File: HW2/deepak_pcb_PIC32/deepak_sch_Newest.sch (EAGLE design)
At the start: 23 parts, among them J1 USB-MB-H

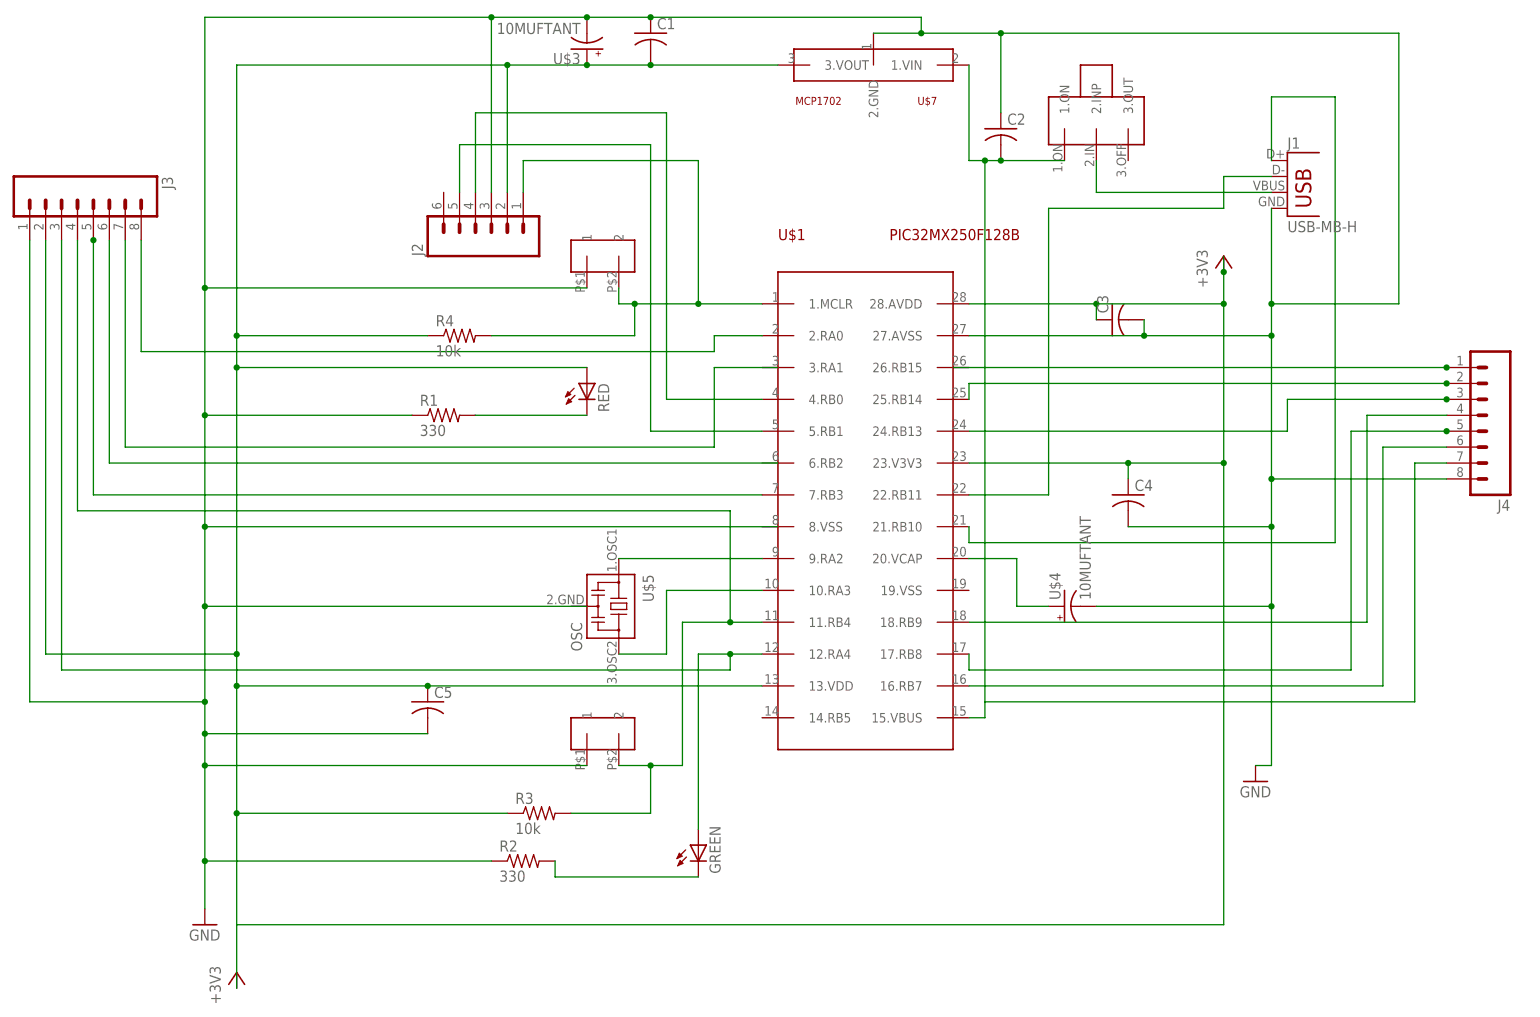
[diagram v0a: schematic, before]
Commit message: Final Schematic. No long connections
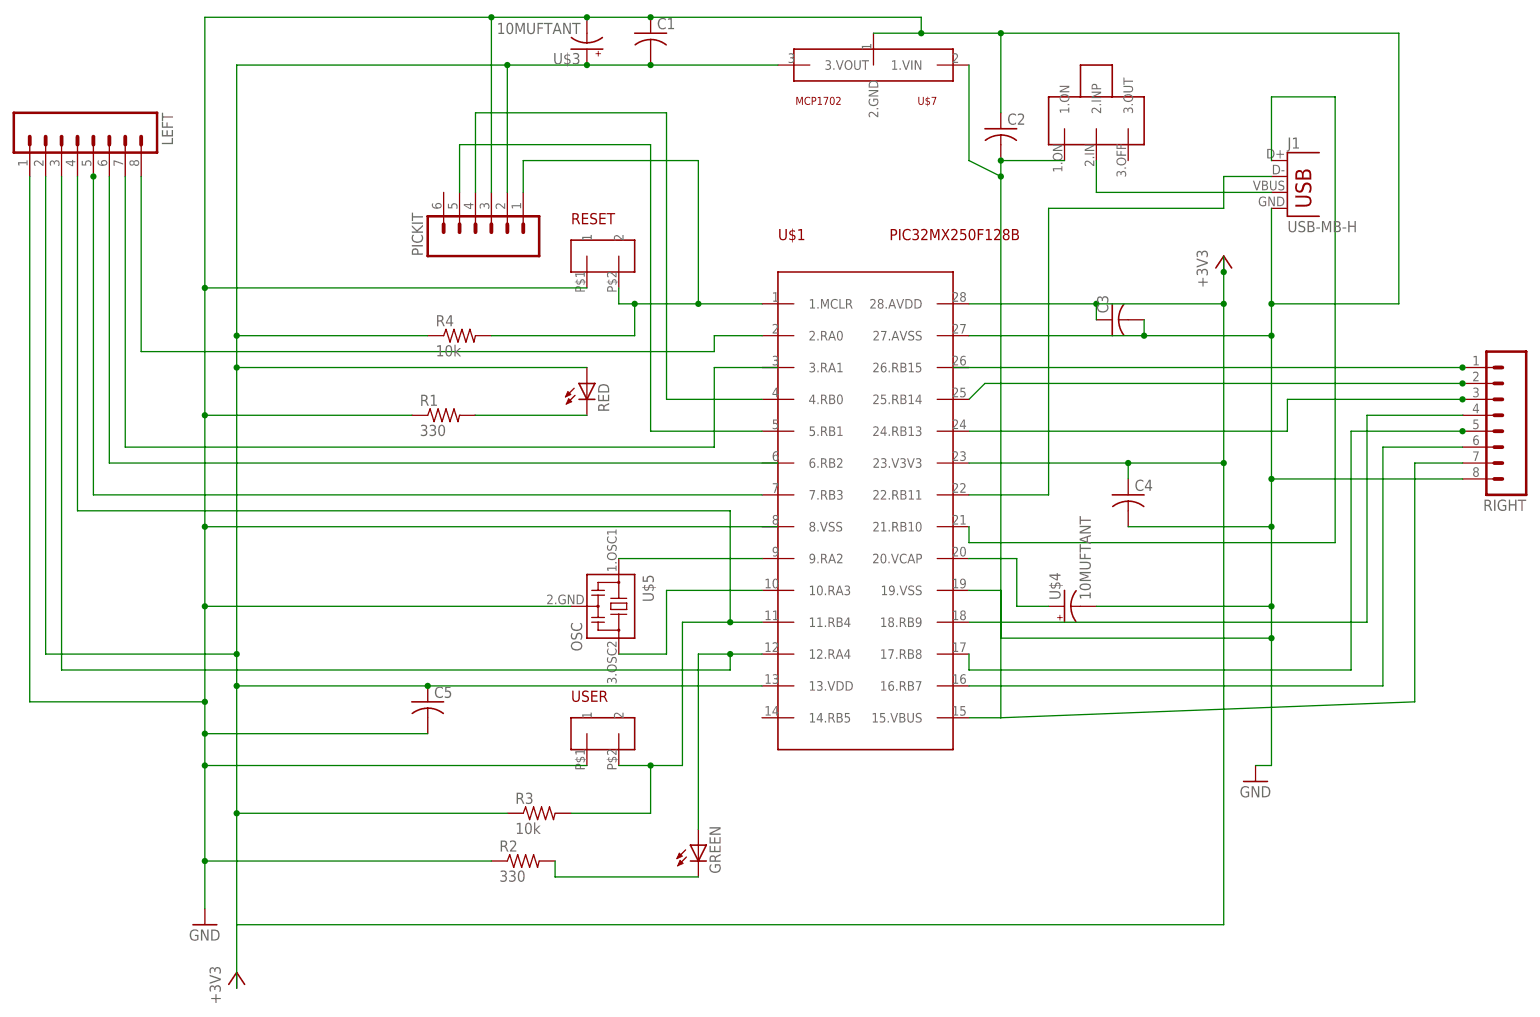
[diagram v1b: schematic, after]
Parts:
- removed J3, J4: (no value), ME433_2:M08
- added LEFT, RIGHT: (no value), ME433_2:M08
- renumbered J2 to PICKIT, U$6 to RESET, U$8 to USER
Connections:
- net +3V3: now also LEFT.2; no longer J3.2
- net GND: now also LEFT.1, RIGHT.8, U$1.19.VSS, U$5.2; no longer J3.1, J4.8
- net N$13: now also LEFT.5; no longer J3.5
- net N$16: now also RIGHT.1; no longer J4.1
- net N$17: now also LEFT.8; no longer J3.8
- net N$18: now also LEFT.7; no longer J3.7
- net N$19: now also LEFT.6; no longer J3.6
- net N$2: now also RIGHT.7; no longer J4.7
- net N$20: now also RIGHT.2; no longer J4.2
- net N$21: now also RIGHT.3; no longer J4.3
- net N$22: now also RIGHT.4; no longer J4.4
- net N$23: now also RIGHT.5; no longer J4.5
- net N$24: now also RIGHT.6; no longer J4.6
- net N$3: now also LEFT.3; no longer J3.3
- net N$8: now also LEFT.4; no longer J3.4
